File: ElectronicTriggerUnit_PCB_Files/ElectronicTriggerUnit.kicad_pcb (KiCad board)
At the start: 2 copper layers, 61.3 x 50 mm, 50 parts, among them IC1 MCP1407-E_SN, IC2 ATTINY814-SSF, IC3 BU4S584G2-TR, J2 Conn_01x05, J4 Conn_01x04, Q1 LC191PTDT, Q2 LKPT30102B-A01, Q3 78-SQRS140ELP, Q4 LC191PTDT, U1 Gnd, U2 12v, U3 GndMotor, U4 Gnd, U5 12v

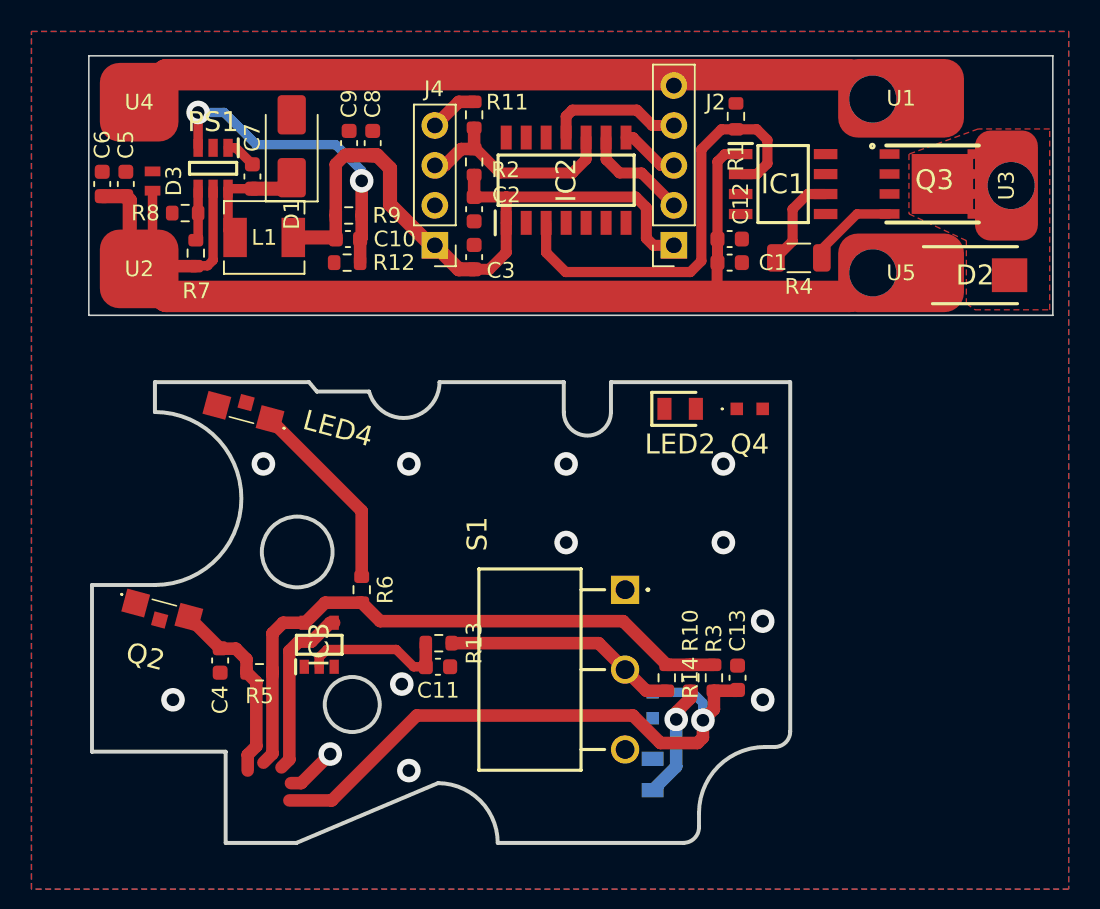
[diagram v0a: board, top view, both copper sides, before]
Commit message: redid ground plane and trace spacing
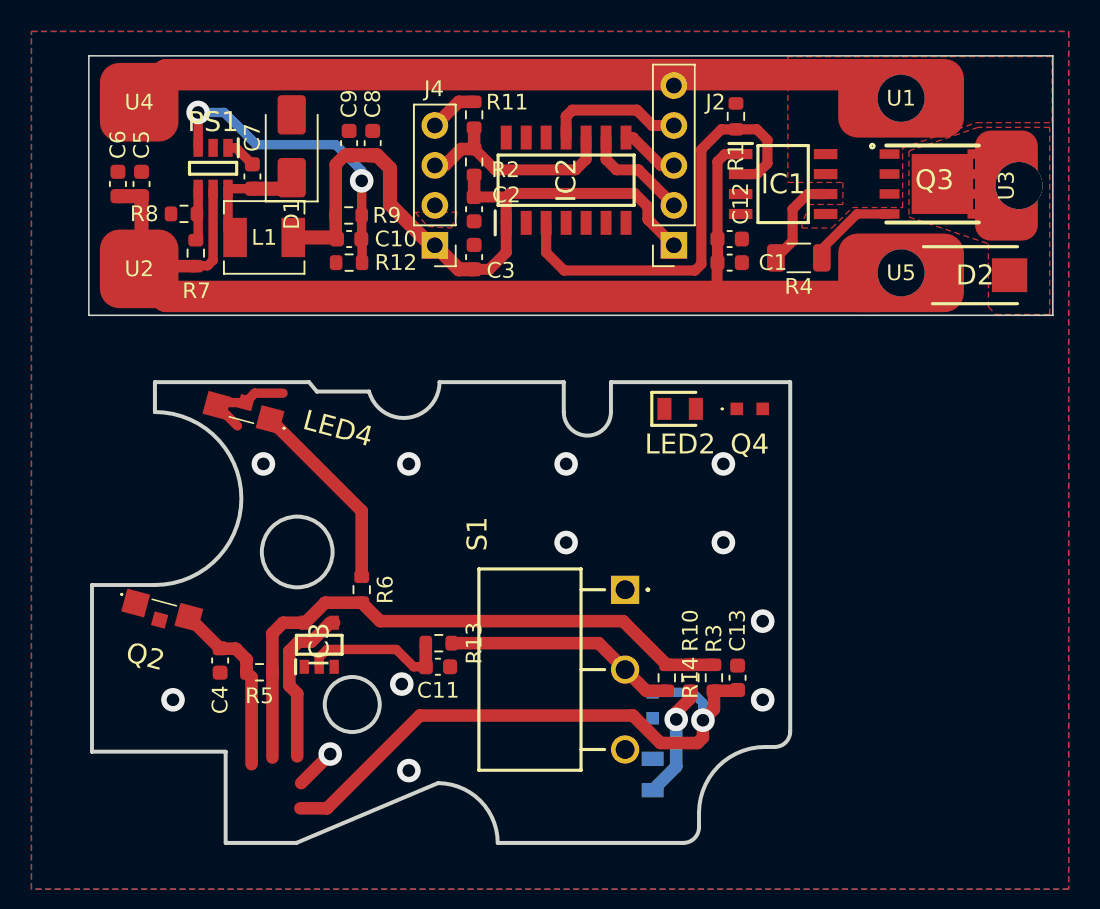
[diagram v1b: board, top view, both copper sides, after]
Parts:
- removed D3: 824045812, SamacSys:TVS_DIODE
- Q3: value 78-SQRS140ELP -> SIR500DP-T1-RE3
- moved C5 1.00 mm to (68.0, 87.2)
- moved C6 1.00 mm to (66.5, 87.2)
- moved R12 0.12 mm to (81.2, 92.2)
- moved R8 0.09 mm to (70.7, 89.1)
- moved C10 0.08 mm to (81.2, 90.7)
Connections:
- LED4 pad 3: (no net) -> GND
- Q2 pad 3: (no net) -> GND
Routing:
- net GND: track 51.9 -> 59.5 mm
- net +12V: track 79.6 -> 75.8 mm
- net +3.3V: track 82.4 -> 81.5 mm
- net /V_Cycle_Out: track 12.3 -> 11.6 mm
- net /trigger_Out: track 11.2 -> 10.5 mm

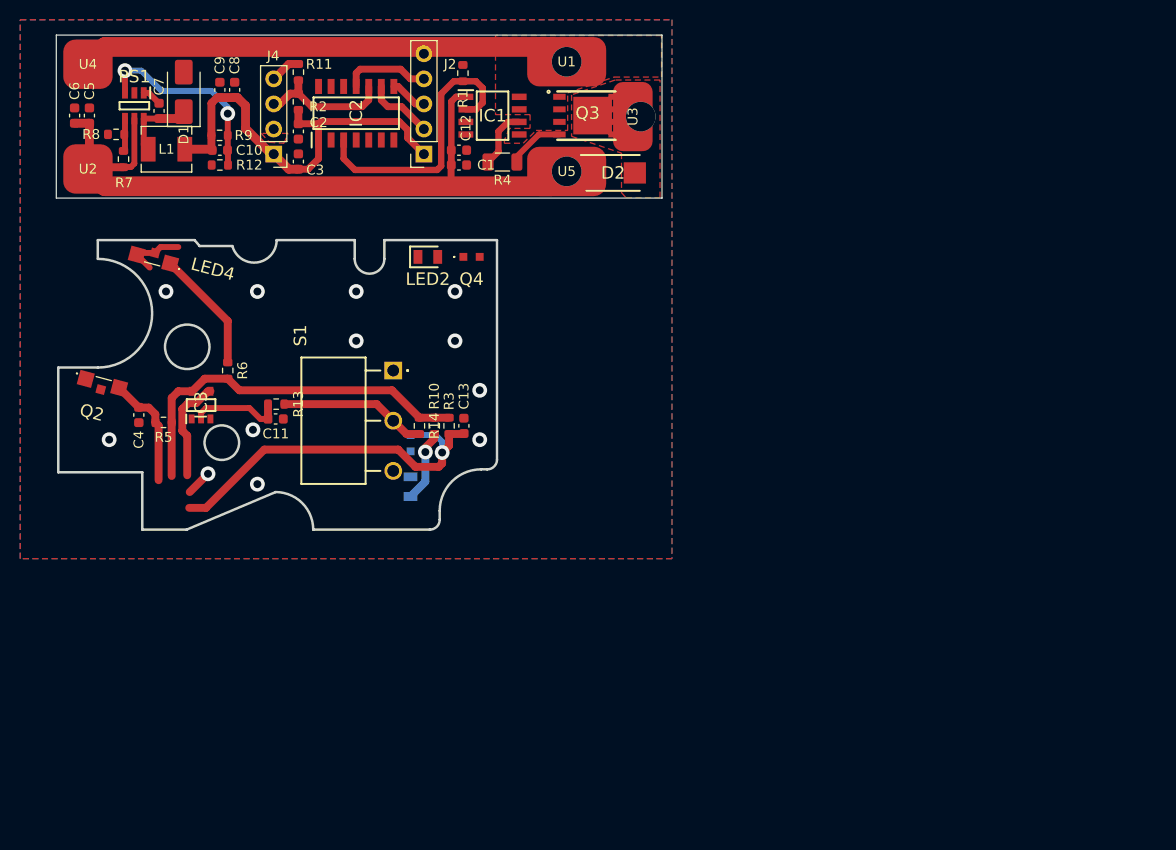
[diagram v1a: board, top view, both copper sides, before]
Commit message: added motor ring
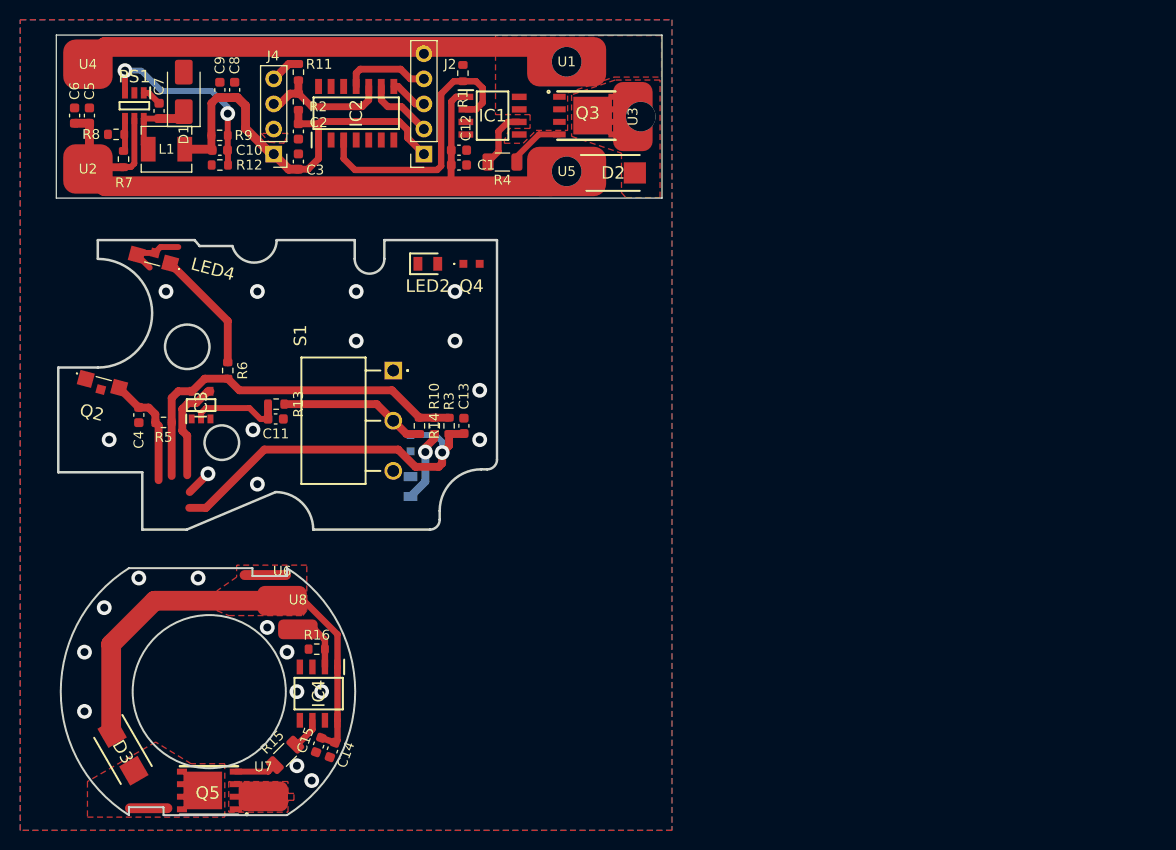
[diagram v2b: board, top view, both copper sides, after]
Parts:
- added C14: 0.1u, Capacitor_SMD:C_0603_1608Metric, F.Cu at (92.6, 151.4)
- added C15: 1u, Capacitor_SMD:C_0603_1608Metric, F.Cu at (91.2, 150.9)
- added D3: SS24, SamacSys:DIOM5436X247N, F.Cu at (71.4, 151.6)
- added IC4: MCP1407-E_SN, SamacSys:SOIC127P600X175-8N, F.Cu at (91.2, 145.7)
- added Q5: SIR500DP-T1-RE3, SamacSys:POWERPAKSO-8, F.Cu at (80.1, 155.5)
- added R15: 10R, Resistor_SMD:R_1206_3216Metric, F.Cu at (87.8, 151.9)
- added R16: 10k, Resistor_SMD:R_0603_1608Metric, F.Cu at (91.0, 141.2)
- added U6: 12v, SamacSys:Copper_Pad, F.Cu at (87.5, 136.3)
- added U7: Gnd, SamacSys:Copper_Pad, F.Cu at (85.6, 156.1)
- added U8: SigIn, SamacSys:Copper_Pad, F.Cu at (89.1, 139.2)
- moved LED2 0.70 mm to (102.2, 102.2)
- moved Q4 0.70 mm to (106.7, 102.2)
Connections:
- LED4 pad 3: GND -> (no net)
- Q2 pad 3: GND -> (no net)
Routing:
- net +12V: track 75.8 -> 127.7 mm
- net /sigIn: track 0.00 -> 5.93 mm
- net Net-(Q5-Pad4): track 0.00 -> 4.21 mm
- net /pwr_motor_ring: track 0.00 -> 3.80 mm
- net Net-(IC4-OUT_1): track 0.00 -> 3.30 mm
- net GND: vias 13 -> 24
- added copper zone on F.Cu, net +12V
- added copper zone on F.Cu, net /pwr_motor_ring
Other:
- board size 61.3 x 50 mm -> 61.3 x 79 mm

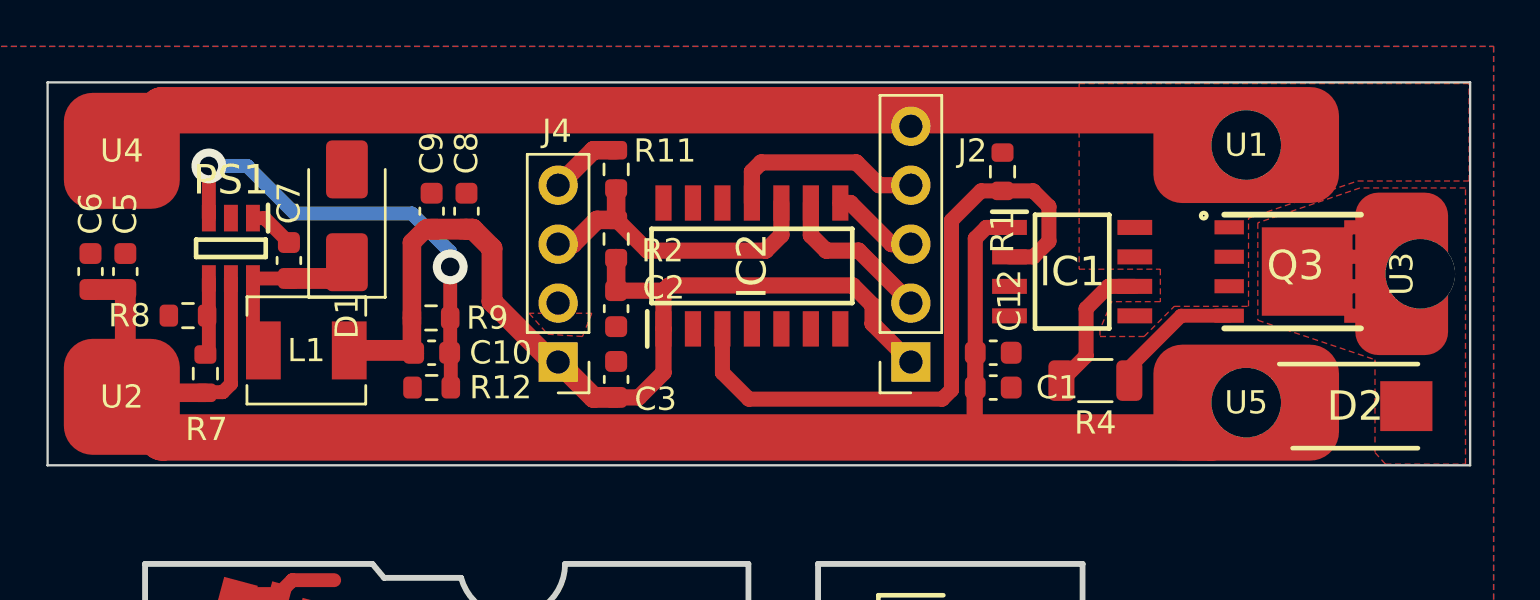
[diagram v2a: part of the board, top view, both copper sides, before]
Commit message: outputs of gate driver needed to be shorted :(
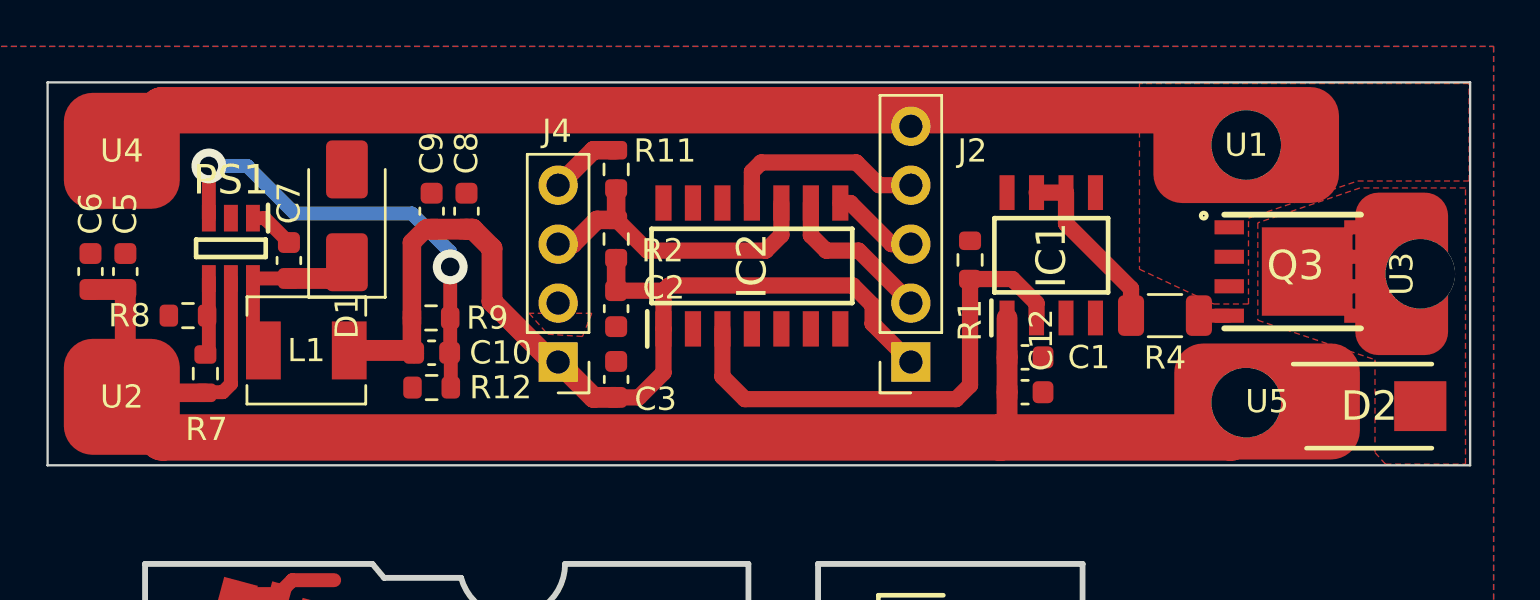
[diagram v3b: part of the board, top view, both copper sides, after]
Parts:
- moved R4 4.10 mm to (112.8, 89.1)
- moved R1 4.05 mm to (104.4, 86.7)
- moved C12 2.18 mm to (106.8, 92.4)
- moved C1 1.89 mm to (106.8, 90.9)
- moved IC1 1.14 mm to (107.9, 86.5), turned to 90 degrees
- moved U5 0.90 mm to (117.2, 92.8)
- moved D2 0.60 mm to (121.6, 93.0)
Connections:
- IC1 pad 7: GND -> Net-(IC1-OUT_1)
- IC1 pad 8: GND -> +12V
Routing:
- net /NMOS: track 28.2 -> 21.9 mm
- net Net-(Q3-Pad4): track 5.79 -> 1.31 mm
- net +12V: track 127.7 -> 123.6 mm
- net Net-(IC1-OUT_1): track 6.04 -> 7.73 mm

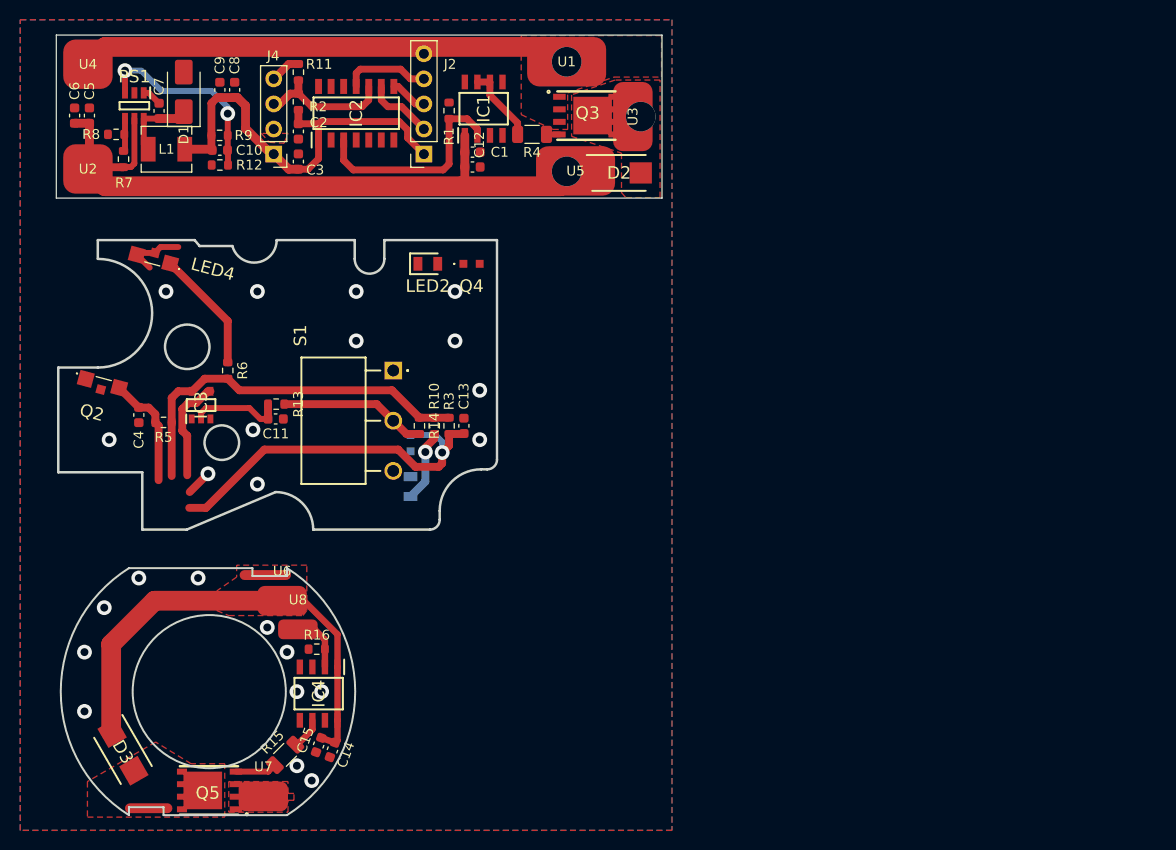
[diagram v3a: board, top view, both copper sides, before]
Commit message: updated code , modified resistors
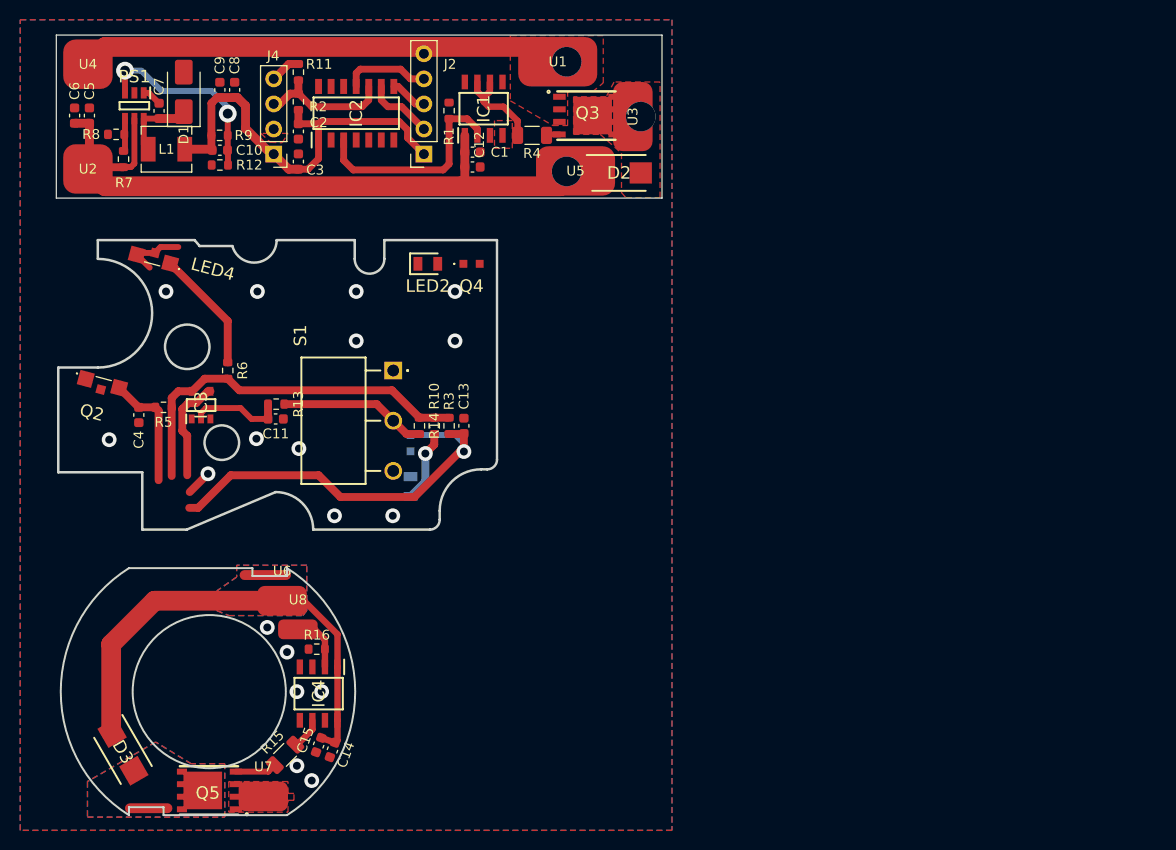
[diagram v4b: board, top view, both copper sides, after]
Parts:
- moved R5 1.53 mm to (75.5, 116.7)
- moved U1 0.90 mm to (115.4, 81.8)
- moved R4 0.10 mm to (112.8, 89.2)
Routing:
- net /Semi_Auto: track 38.3 -> 41.9 mm
- net Net-(IC1-OUT_1): track 7.73 -> 9.73 mm
- net GND: track 59.5 -> 58.6 mm, vias 24 -> 19
- added copper zone on B.Cu, net +12V
- added copper zone on B.Cu, net /pwr_motor_ring
